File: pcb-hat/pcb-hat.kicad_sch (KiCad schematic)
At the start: 30 parts, among them U1 INA219AxD, U3 AOZ6605PI-1

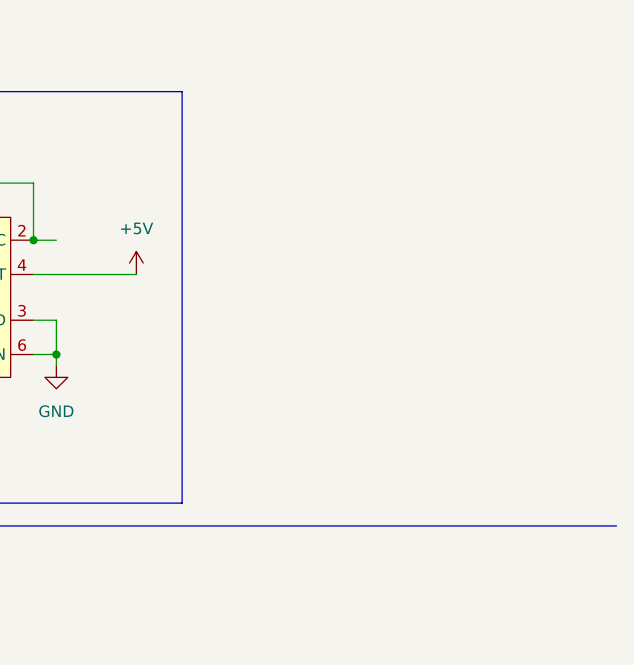
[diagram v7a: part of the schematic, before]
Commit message: LED added
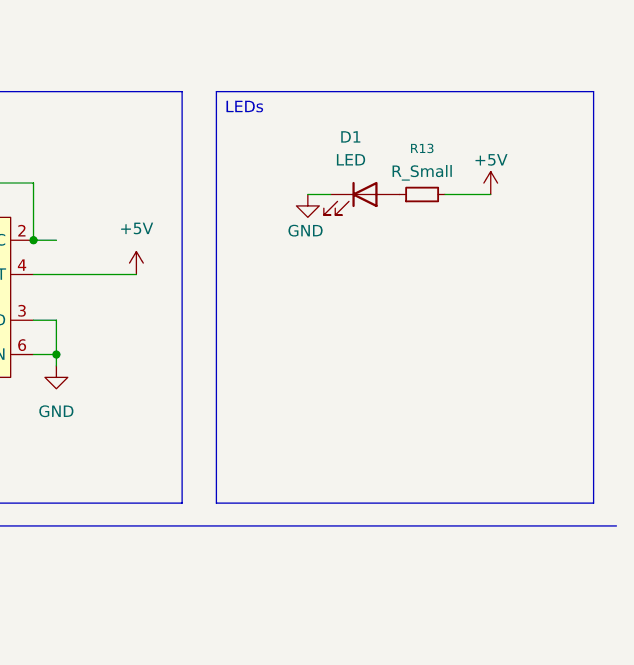
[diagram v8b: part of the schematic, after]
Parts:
- added D1: LED, symbol Device:LED
- added R13: R_Small, symbol Device:R_Small
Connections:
- net +5V: now also R13.2
- net GND: now also D1.1 (K)
- new net: D1.2 (A), R13.1
